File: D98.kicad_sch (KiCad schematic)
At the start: 34 parts, among them J1 Conn_01x08, J2 Conn_01x06, J3 Conn_01x06, J4 Conn_01x06, J5 Conn_01x05, J6 Conn_01x04, J7 Conn_01x02, U1 YAAJ_BluePill_SWD_Breakout, U2 Poka Yoke

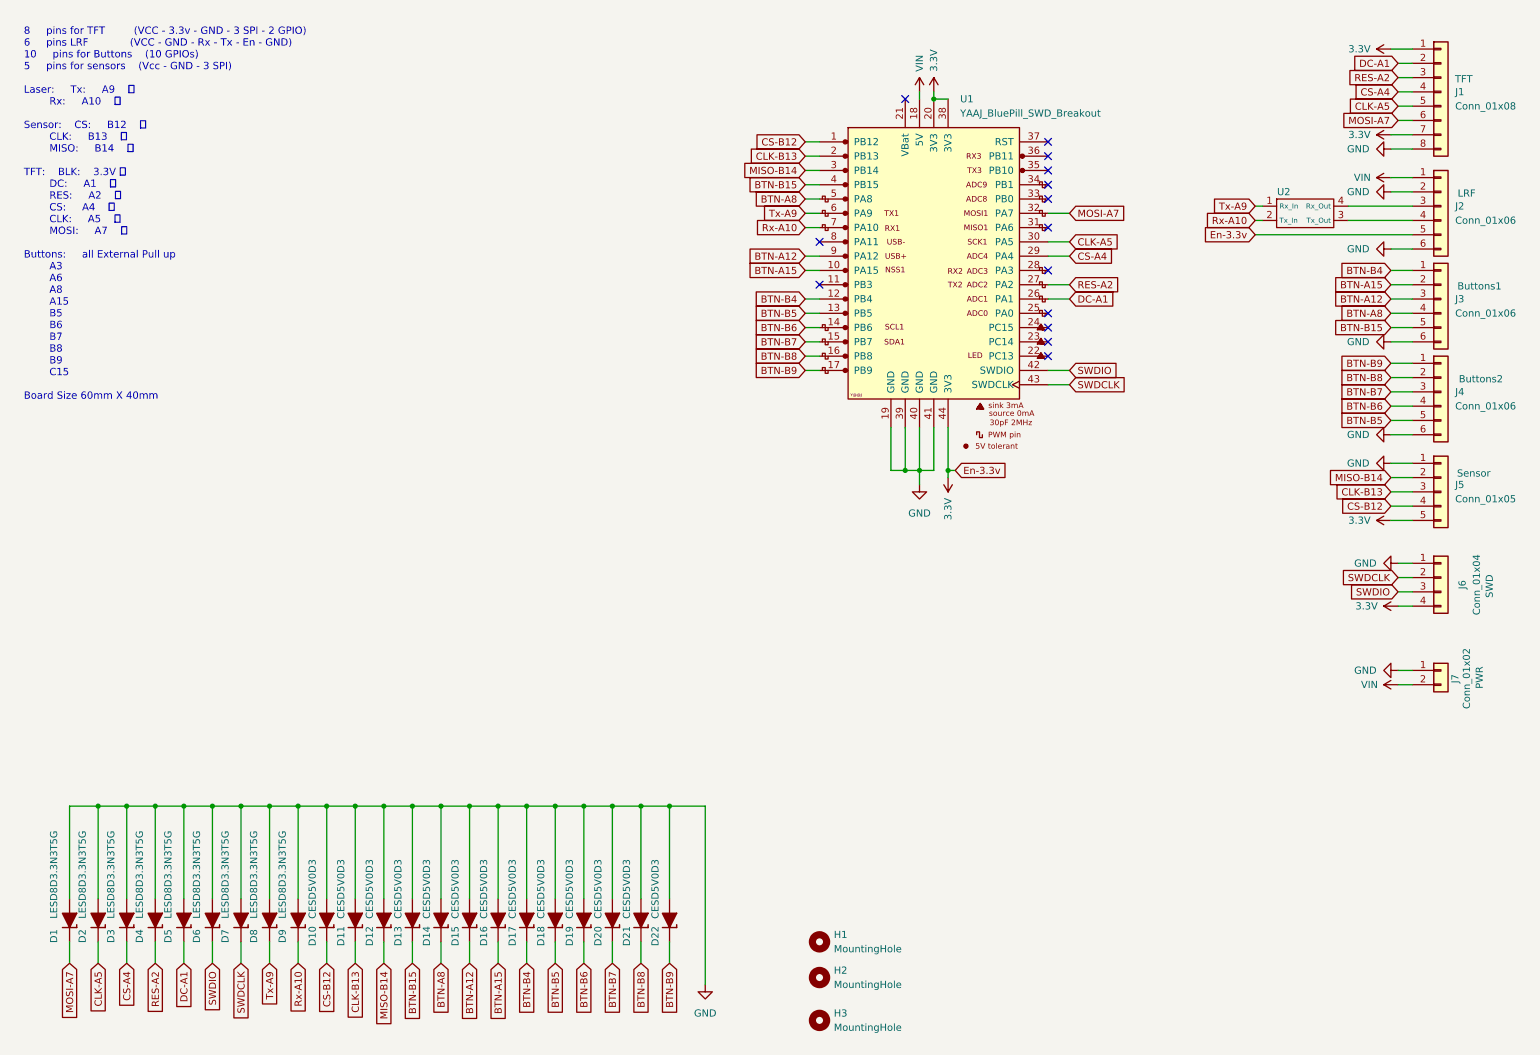
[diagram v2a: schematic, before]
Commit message: Feat & Edit: changer the position of the TVSes & adding Connector.
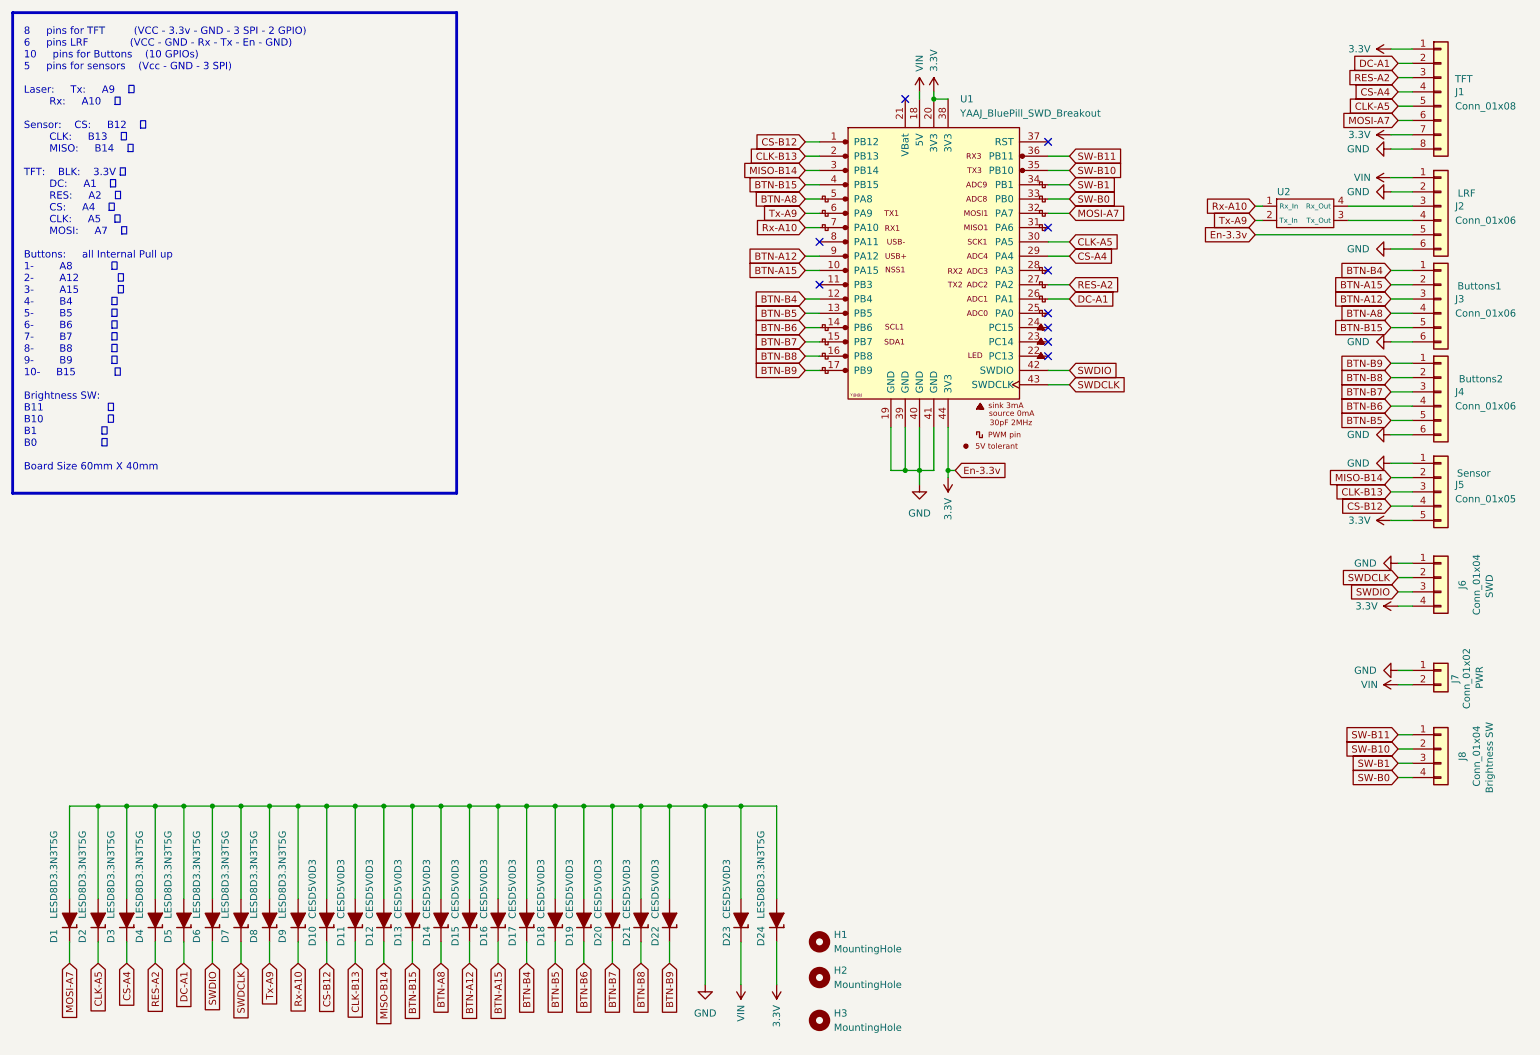
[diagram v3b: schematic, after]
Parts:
- added D23: CESD5V0D3, Diode_SMD:D_SOD-323_HandSoldering, symbol Diode:D_TVS_Unidirectional_Generic
- added D24: LESD8D3.3N3T5G, Diode_SMD:D_SOD-882D, symbol PCM_Diode_TVS_AKL:LESD8D3.3CAT5G
- added J8: Conn_01x04, Connector_JST:JST_XH_S4B-XH-A-1_1x04_P2.50mm_Horizontal, symbol Connector_Generic:Conn_01x04
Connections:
- net 3.3V: now also D24.1 (K)
- net GND: now also D23.2 (A), D24.2 (A)
- net Rx-A10: now also U2.1 (Rx_In); no longer U2.2 (Tx_In)
- net Tx-A9: now also U2.2 (Tx_In); no longer U2.1 (Rx_In)
- net VIN: now also D23.1 (K)
- net SW-B0: now reaches U1.33 (PB0)
- net SW-B0: now also J8.4 (Pin_4)
- net SW-B1: now reaches U1.34 (PB1)
- net SW-B1: now also J8.3 (Pin_3)
- net SW-B10: now reaches U1.35 (PB10)
- net SW-B10: now also J8.2 (Pin_2)
- net SW-B11: now reaches U1.36 (PB11)
- net SW-B11: now also J8.1 (Pin_1)
- no-connect marks 14 -> 10
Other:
- note added: "8 pins for TFT (VCC - 3.3v - GND - 3 SPI - 2 GPIO) 6 pins LRF (VCC - GND - Rx - Tx - En - GND) 10 pins for Buttons (10 GPIOs) 5 pins for sensors (Vcc - GND - 3 SPI) Laser: Tx: A9 ✅ Rx: A10 ✅ Sensor: CS: B12 ✅ CLK: B13 ✅ MISO: B14 ✅ TFT: BLK: 3.3V ✅ DC: A1 ✅ RES: A2 ✅ CS: A4 ✅ CLK: A5 ✅ MOSI: A7 ✅ Buttons: all Internal Pull up 1- A8 ✅ 2- A12 ✅ 3- A15 ✅ 4- B4 ✅ 5- B5 ✅ 6- B6 ✅ 7- B7 ✅ 8- B8 ✅ 9- B9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"
- note removed: "8 pins for TFT (VCC - 3.3v - GND - 3 SPI - 2 GPIO) 6 pins LRF (VCC - GND - Rx - Tx - En - GND) 10 pins for Buttons (10 GPIOs) 5 pins for sensors (Vcc - GND - 3 SPI) Laser: Tx: A9 ✅ Rx: A10 ✅ Sensor: CS: B12 ✅ CLK: B13 ✅ MISO: B14 ✅ TFT: BLK: 3.3V ✅ DC: A1 ✅ RES: A2 ✅ CS: A4 ✅ CLK: A5 ✅ MOSI: A7 ✅ Buttons: all External Pull up A3 A6 A8 A15 B5 B6 B7 B8 B9 C15 Board Size 60mm X 40mm"
- company: (none) -> AIO
- title: (none) -> stm32 connection Borad

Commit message: Fix: Changing the EN pin of TFT from always full Brightness to becontrolled Via PWM Pin.
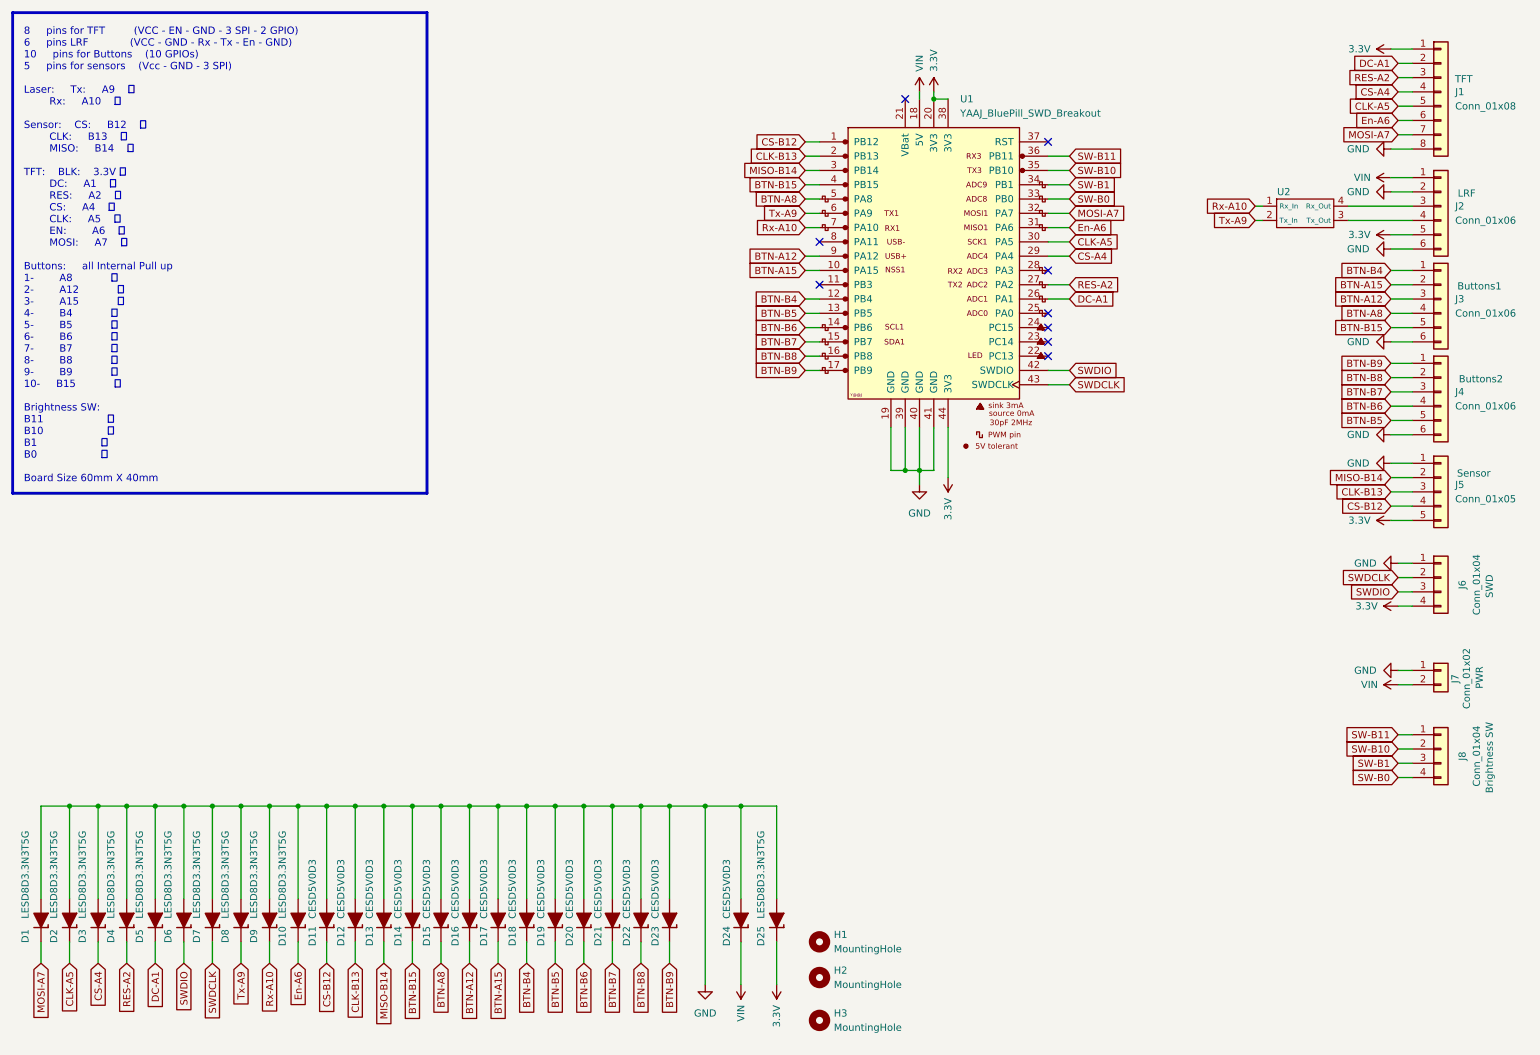
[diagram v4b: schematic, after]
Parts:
- added D10: LESD8D3.3N3T5G, Diode_SMD:D_SOD-882D, symbol PCM_Diode_TVS_AKL:LESD8D3.3CAT5G
- renumbered D10 to D11, D11 to D12, D12 to D13, D13 to D14, D14 to D15, D15 to D16, D16 to D17, D17 to D18, D18 to D19, D19 to D20, D20 to D21, D21 to D22, D22 to D23, D23 to D24, D24 to D25
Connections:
- net 3.3V: no longer J1.7 (Pin_7)
- net GND: now also D10.2 (A)
- net MOSI-A7: now also J1.7 (Pin_7); no longer J1.6 (Pin_6)
- net En-A6: now reaches U1.31 (PA6)
- net En-A6: now also J1.6 (Pin_6), D10.1 (K)
- no-connect marks 10 -> 9
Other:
- note added: "8 pins for TFT (VCC - EN - GND - 3 SPI - 2 GPIO) 6 pins LRF (VCC - GND - Rx - Tx - En - GND) 10 pins for Buttons (10 GPIOs) 5 pins for sensors (Vcc - GND - 3 SPI) Laser: Tx: A9 ✅ Rx: A10 ✅ Sensor: CS: B12 ✅ CLK: B13 ✅ MISO: B14 ✅ TFT: BLK: 3.3V ✅ DC: A1 ✅ RES: A2 ✅ CS: A4 ✅ CLK: A5 ✅ EN: A6 ✅ MOSI: A7 ✅ Buttons: all Internal Pull up 1- A8 ✅ 2- A12 ✅ 3- A15 ✅ 4- B4 ✅ 5- B5 ✅ 6- B6 ✅ 7- B7 ✅ 8- B8 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"
- note removed: "8 pins for TFT (VCC - 3.3v - GND - 3 SPI - 2 GPIO) 6 pins LRF (VCC - GND - Rx - Tx - En - GND) 10 pins for Buttons (10 GPIOs) 5 pins for sensors (Vcc - GND - 3 SPI) Laser: Tx: A9 ✅ Rx: A10 ✅ Sensor: CS: B12 ✅ CLK: B13 ✅ MISO: B14 ✅ TFT: BLK: 3.3V ✅ DC: A1 ✅ RES: A2 ✅ CS: A4 ✅ CLK: A5 ✅ MOSI: A7 ✅ Buttons: all Internal Pull up 1- A8 ✅ 2- A12 ✅ 3- A15 ✅ 4- B4 ✅ 5- B5 ✅ 6- B6 ✅ 7- B7 ✅ 8- B8 ✅ 9- B9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"
- moved on the sheet: D1, D2, D3, D4, D5, D6, D7, D8, D9

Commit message: fix: changed the EN pin GPIO agian from A6 to A3 because A6 is MSIO.
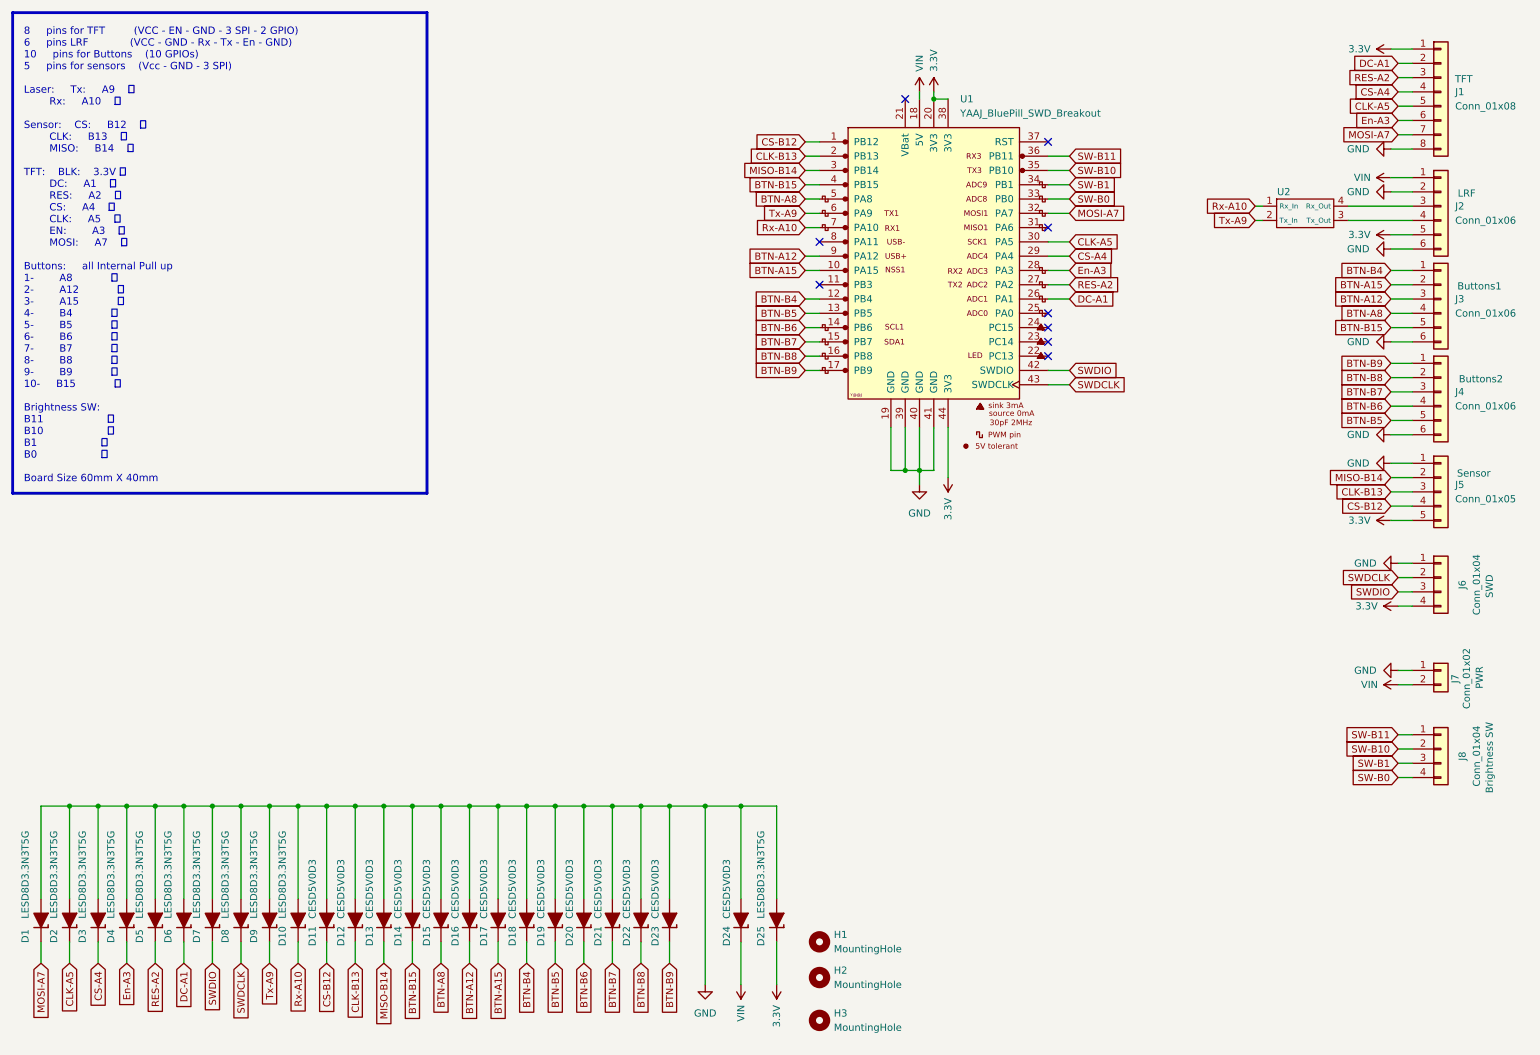
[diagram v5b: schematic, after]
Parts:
- renumbered D9 to D10, D10 to D4, D4 to D5, D5 to D6, D6 to D7, D7 to D8, D8 to D9
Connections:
- net En-A3: now reaches U1.28 (PA3)
- net En-A3: now also D4.1 (K), J1.6 (Pin_6)
- removed net En-A6: D4.1 (K), J1.6 (Pin_6), U1.31 (PA6)
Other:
- note added: "8 pins for TFT (VCC - EN - GND - 3 SPI - 2 GPIO) 6 pins LRF (VCC - GND - Rx - Tx - En - GND) 10 pins for Buttons (10 GPIOs) 5 pins for sensors (Vcc - GND - 3 SPI) Laser: Tx: A9 ✅ Rx: A10 ✅ Sensor: CS: B12 ✅ CLK: B13 ✅ MISO: B14 ✅ TFT: BLK: 3.3V ✅ DC: A1 ✅ RES: A2 ✅ CS: A4 ✅ CLK: A5 ✅ EN: A3 ✅ MOSI: A7 ✅ Buttons: all Internal Pull up 1- A8 ✅ 2- A12 ✅ 3- A15 ✅ 4- B4 ✅ 5- B5 ✅ 6- B6 ✅ 7- B7 ✅ 8- B8 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"
- note removed: "8 pins for TFT (VCC - EN - GND - 3 SPI - 2 GPIO) 6 pins LRF (VCC - GND - Rx - Tx - En - GND) 10 pins for Buttons (10 GPIOs) 5 pins for sensors (Vcc - GND - 3 SPI) Laser: Tx: A9 ✅ Rx: A10 ✅ Sensor: CS: B12 ✅ CLK: B13 ✅ MISO: B14 ✅ TFT: BLK: 3.3V ✅ DC: A1 ✅ RES: A2 ✅ CS: A4 ✅ CLK: A5 ✅ EN: A6 ✅ MOSI: A7 ✅ Buttons: all Internal Pull up 1- A8 ✅ 2- A12 ✅ 3- A15 ✅ 4- B4 ✅ 5- B5 ✅ 6- B6 ✅ 7- B7 ✅ 8- B8 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"
- moved on the sheet: D10, D4, D5, D6, D7, D8, D9

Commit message: Feat: Change the Rounting of Tracks and the silkscreen.
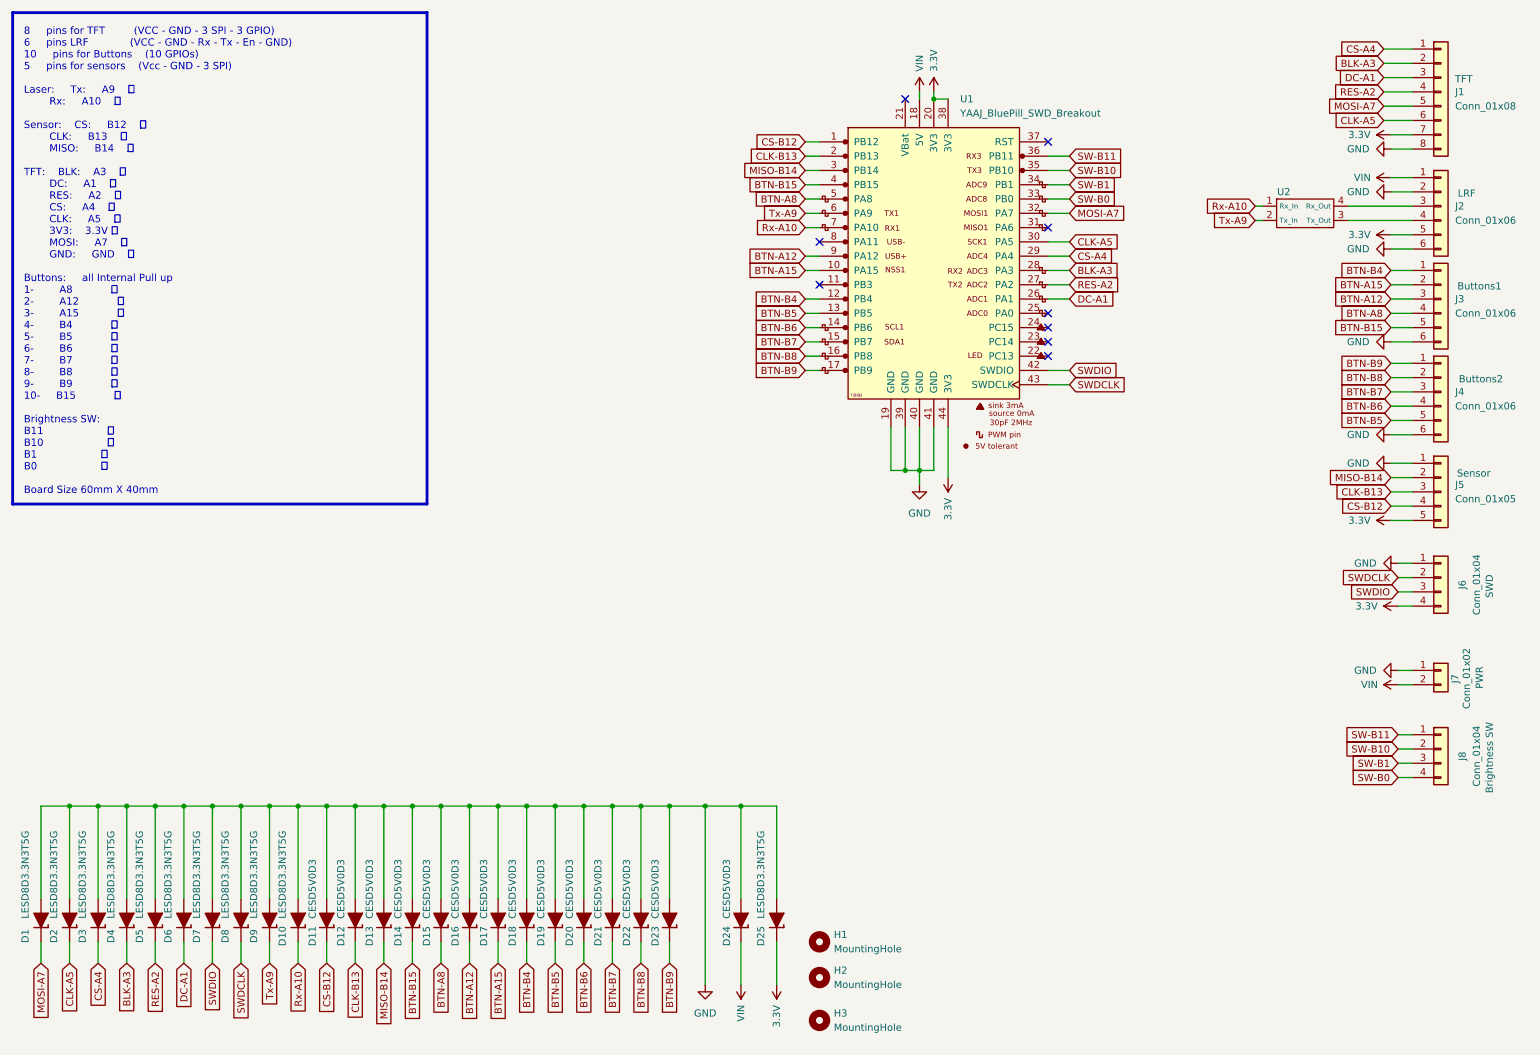
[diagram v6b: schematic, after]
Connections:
- net 3.3V: now also J1.7 (Pin_7); no longer J1.1 (Pin_1)
- net CLK-A5: now also J1.6 (Pin_6); no longer J1.5 (Pin_5)
- net CS-A4: now also J1.1 (Pin_1); no longer J1.4 (Pin_4)
- net DC-A1: now also J1.3 (Pin_3); no longer J1.2 (Pin_2)
- net MOSI-A7: now also J1.5 (Pin_5); no longer J1.7 (Pin_7)
- net RES-A2: now also J1.4 (Pin_4); no longer J1.3 (Pin_3)
- net En-A3 renamed BLK-A3
- net BLK-A3: now also J1.2 (Pin_2); no longer J1.6 (Pin_6)
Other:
- note added: "8 pins for TFT (VCC - GND - 3 SPI - 3 GPIO) 6 pins LRF (VCC - GND - Rx - Tx - En - GND) 10 pins for Buttons (10 GPIOs) 5 pins for sensors (Vcc - GND - 3 SPI) Laser: Tx: A9 ✅ Rx: A10 ✅ Sensor: CS: B12 ✅ CLK: B13 ✅ MISO: B14 ✅ TFT: BLK: A3 ✅ DC: A1 ✅ RES: A2 ✅ CS: A4 ✅ CLK: A5 ✅ 3V3: 3.3V ✅ MOSI: A7 ✅ GND: GND ✅ Buttons: all Internal Pull up 1- A8 ✅ 2- A12 ✅ 3- A15 ✅ 4- B4 ✅ 5- B5 ✅ 6- B6 ✅ 7- B7 ✅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"
- note removed: "8 pins for TFT (VCC - EN - GND - 3 SPI - 2 GPIO) 6 pins LRF (VCC - GND - Rx - Tx - En - GND) 10 pins for Buttons (10 GPIOs) 5 pins for sensors (Vcc - GND - 3 SPI) Laser: Tx: A9 ✅ Rx: A10 ✅ Sensor: CS: B12 ✅ CLK: B13 ✅ MISO: B14 ✅ TFT: BLK: 3.3V ✅ DC: A1 ✅ RES: A2 ✅ CS: A4 ✅ CLK: A5 ✅ EN: A3 ✅ MOSI: A7 ✅ Buttons: all Internal Pull up 1- A8 ✅ 2- A12 ✅ 3- A15 ✅ 4- B4 ✅ 5- B5 ✅ 6- B6 ✅ 7- B7 ✅ 8- B8 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"
